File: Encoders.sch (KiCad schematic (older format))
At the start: 12 parts, among them J10 Conn_01x04, J7 Conn_01x04, J8 Conn_01x04, J9 Conn_01x04, U10 AS5045B, U11 AS5045B

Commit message: Removed encoders from schematic as moved to the new project
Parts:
- removed C20, C21: 10uF, Capacitor_SMD:C_0603_1608Metric, symbol Device:C_Small
- removed C22, C23: 0.1uF, Capacitor_SMD:C_0402_1005Metric, symbol Device:C_Small
- removed J10, J9: Conn_01x04, Connector_PinHeader_1.00mm:PinHeader_1x04_P1.00mm_Vertical_SMD_Pin1Left, symbol Connector_Generic:Conn_01x04
- removed R27, R28: 10K, Resistor_SMD:R_0402_1005Metric, symbol Device:R_Small
- removed U10, U11: AS5045B, Package_SO:SSOP-16_5.3x6.2mm_P0.65mm, symbol Sensor_Magnetic:AS5045B
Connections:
- wire segments 42 -> 12
- no-connect marks 14 -> 0

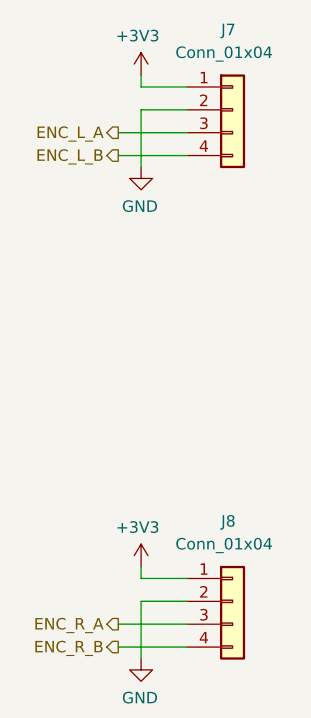
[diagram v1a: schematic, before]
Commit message: Finished encoders, added XSHUT pullups
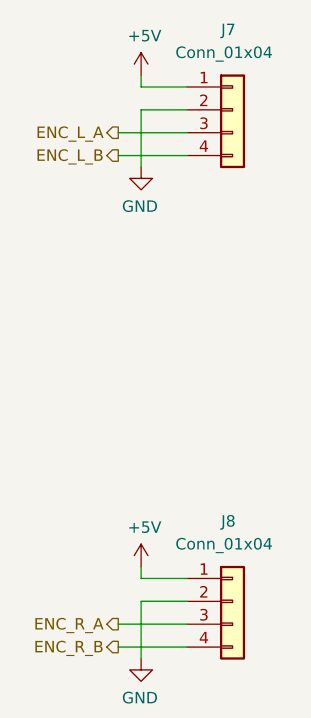
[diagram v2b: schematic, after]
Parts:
- J7, J8: footprint Connector_PinHeader_1.00mm:PinHeader_1x04_P1.00mm_Vertical_SMD_Pin1Left -> connector_brd2brd:01x04_1.0x0.5mm_SMD
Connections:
- net +3V3 renamed +5V
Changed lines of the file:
@@
 F 0 "J7" H 3950 2650 50  0000 L CNN
 F 1 "Conn_01x04" H 3750 2550 50  0000 L CNN
-F 2 "Connector_PinHeader_1.00mm:PinHeader_1x04_P1.00mm_Vertical_SMD_Pin1Left" H 4000 2300 50  0001 C CNN
+F 2 "connector_brd2brd:01x04_1.0x0.5mm_SMD" H 4000 2300 50  0001 C CNN
 F 3 "~" H 4000 2300 50  0001 C CNN
 	1    4000 2300
@@
 F 0 "J8" H 3950 4800 50  0000 L CNN
 F 1 "Conn_01x04" H 3750 4700 50  0000 L CNN
-F 2 "Connector_PinHeader_1.00mm:PinHeader_1x04_P1.00mm_Vertical_SMD_Pin1Left" H 4000 4450 50  0001 C CNN
+F 2 "connector_brd2brd:01x04_1.0x0.5mm_SMD" H 4000 4450 50  0001 C CNN
 F 3 "~" H 4000 4450 50  0001 C CNN
 	1    4000 4450
@@
 Wire Wire Line
 	3800 2200 3600 2200
-$Comp
-L power:+3V3 #PWR0170
-U 1 1 5E69736C
-P 3600 2150
-F 0 "#PWR0170" H 3600 2000 50  0001 C CNN
-F 1 "+3V3" H 3615 2323 50  0000 C CNN
-F 2 "" H 3600 2150 50  0001 C CNN
-F 3 "" H 3600 2150 50  0001 C CNN
-	1    3600 2150
-	-1   0    0    -1
-$EndComp
 Wire Wire Line
 	3600 2150 3600 2200
@@
 Wire Wire Line
 	3800 4350 3600 4350
-$Comp
-L power:+3V3 #PWR0172
-U 1 1 5E69E17E
-P 3600 4300
-F 0 "#PWR0172" H 3600 4150 50  0001 C CNN
-F 1 "+3V3" H 3615 4473 50  0000 C CNN
-F 2 "" H 3600 4300 50  0001 C CNN
-F 3 "" H 3600 4300 50  0001 C CNN
-	1    3600 4300
-	-1   0    0    -1
-$EndComp
 Wire Wire Line
 	3600 4300 3600 4350
@@
 Text HLabel 3500 4650 0    50   Output ~ 0
 ENC_R_B
+$Comp
+L power:+5V #PWR0170
+U 1 1 5E67CEDB
+P 3600 2150
+F 0 "#PWR0170" H 3600 2000 50  0001 C CNN
+F 1 "+5V" H 3615 2323 50  0000 C CNN
+F 2 "" H 3600 2150 50  0001 C CNN
+F 3 "" H 3600 2150 50  0001 C CNN
+	1    3600 2150
+	1    0    0    -1
+$EndComp
+$Comp
+L power:+5V #PWR0172
+U 1 1 5E67D650
+P 3600 4300
+F 0 "#PWR0172" H 3600 4150 50  0001 C CNN
+F 1 "+5V" H 3615 4473 50  0000 C CNN
+F 2 "" H 3600 4300 50  0001 C CNN
+F 3 "" H 3600 4300 50  0001 C CNN
+	1    3600 4300
+	1    0    0    -1
+$EndComp
 $EndSCHEMATC
